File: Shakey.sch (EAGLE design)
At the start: 84 parts, among them CN1 MicroUSB, U1 ATMEGA32U4-AU, U2 ICM-20689, U3 AP2210K-3.3TRG1, U4 LM75AD, Y1 16Mhz

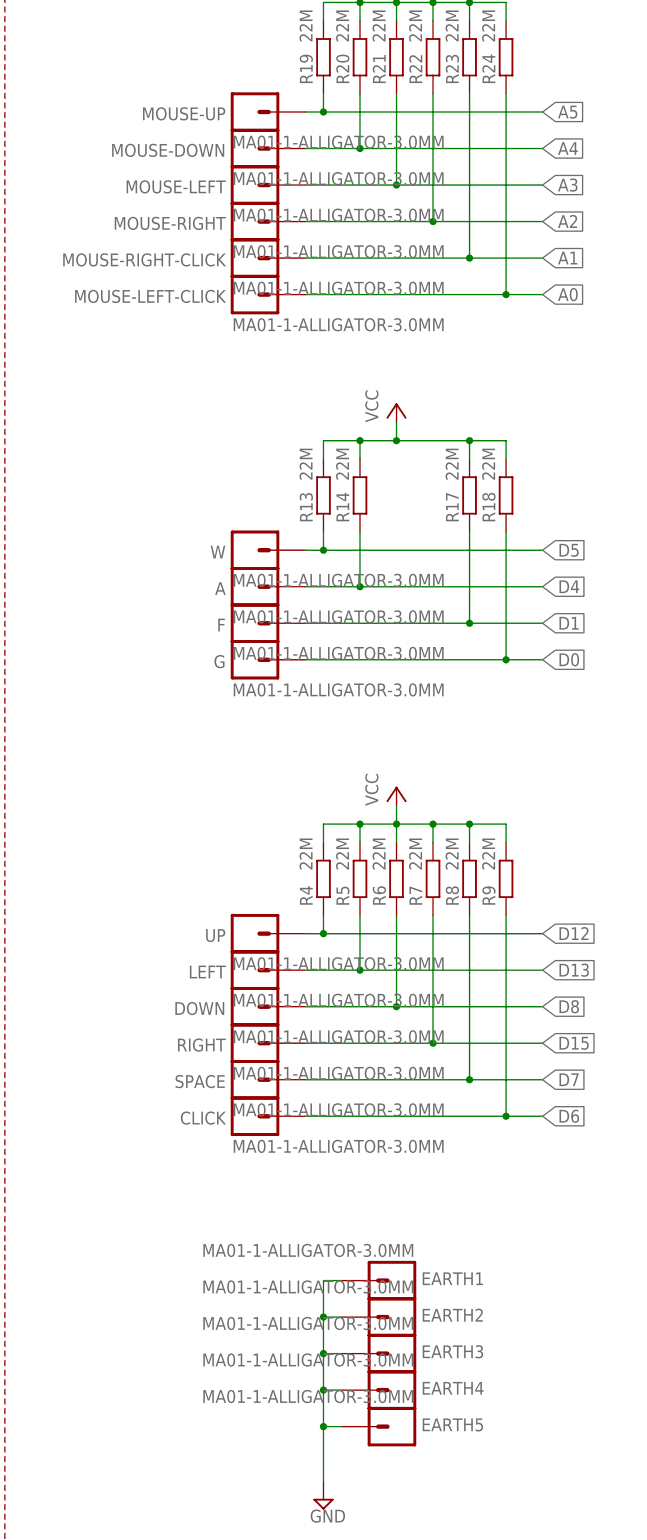
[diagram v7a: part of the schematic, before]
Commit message: added part value for P&P
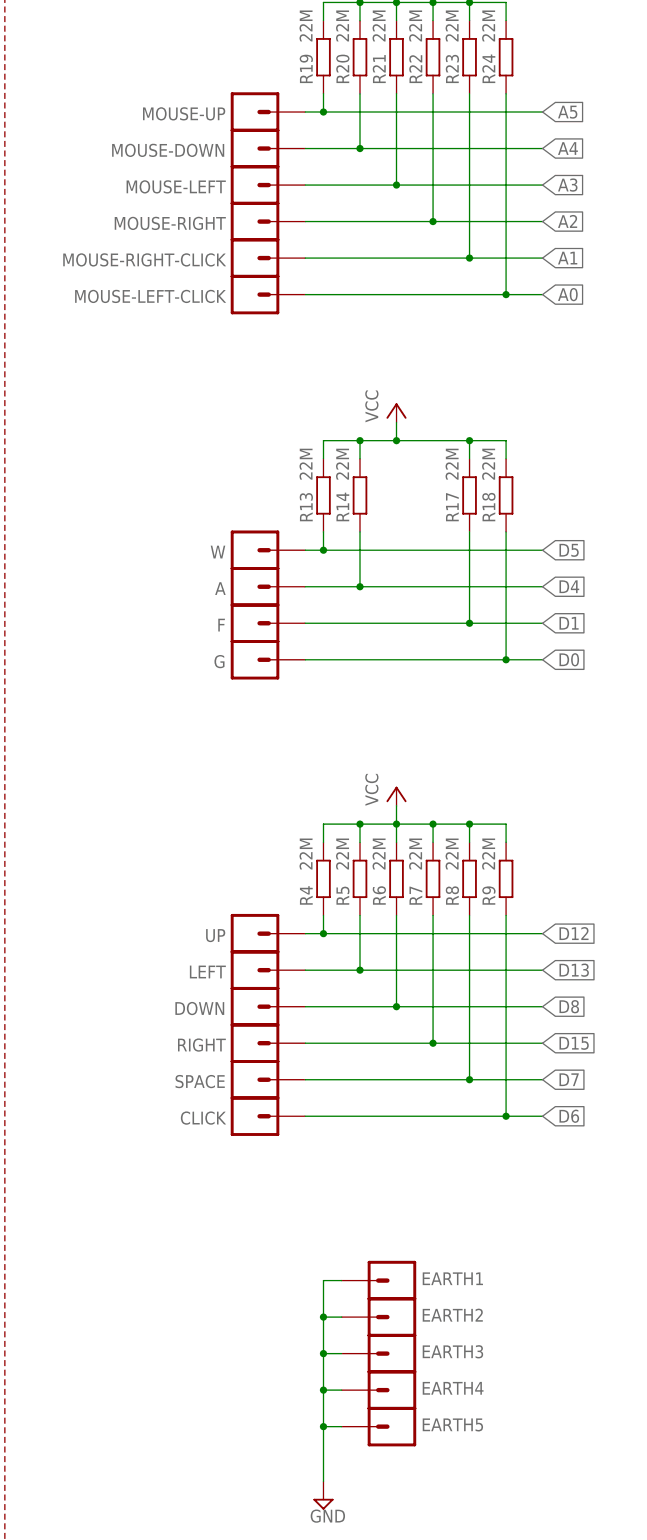
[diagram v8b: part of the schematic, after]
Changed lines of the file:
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@@
 </part>
 <part name="P+3" library="supply1" deviceset="VCC" device=""/>
-<part name="UP" library="SixthLogic" deviceset="MA01-1-ALLIGATOR" device="-3.0MM" value="MA01-1-ALLIGATOR-3.0MM"/>
-<part name="LEFT" library="SixthLogic" deviceset="MA01-1-ALLIGATOR" device="-3.0MM" value="MA01-1-ALLIGATOR-3.0MM"/>
-<part name="DOWN" library="SixthLogic" deviceset="MA01-1-ALLIGATOR" device="-3.0MM" value="MA01-1-ALLIGATOR-3.0MM"/>
-<part name="RIGHT" library="SixthLogic" deviceset="MA01-1-ALLIGATOR" device="-3.0MM" value="MA01-1-ALLIGATOR-3.0MM"/>
-<part name="SPACE" library="SixthLogic" deviceset="MA01-1-ALLIGATOR" device="-3.0MM" value="MA01-1-ALLIGATOR-3.0MM"/>
-<part name="CLICK" library="SixthLogic" deviceset="MA01-1-ALLIGATOR" device="-3.0MM" value="MA01-1-ALLIGATOR-3.0MM"/>
+<part name="UP" library="SixthLogic" deviceset="MA01-1-ALLIGATOR" device="-3.0MM" value=""/>
+<part name="LEFT" library="SixthLogic" deviceset="MA01-1-ALLIGATOR" device="-3.0MM" value=""/>
+<part name="DOWN" library="SixthLogic" deviceset="MA01-1-ALLIGATOR" device="-3.0MM" value=""/>
+<part name="RIGHT" library="SixthLogic" deviceset="MA01-1-ALLIGATOR" device="-3.0MM" value=""/>
+<part name="SPACE" library="SixthLogic" deviceset="MA01-1-ALLIGATOR" device="-3.0MM" value=""/>
+<part name="CLICK" library="SixthLogic" deviceset="MA01-1-ALLIGATOR" device="-3.0MM" value=""/>
 <part name="R4" library="rcl" deviceset="R-EU_" device="R0603" value="22M">
 <attribute name="DESCRIPTION" value="RES SMD 22M OHM 10% 1/10W 0603"/>
@@
 <attribute name="URL" value="https://www.digikey.com/product-detail/en/panasonic-electronic-components/ERJ-3GEYK226V/P22MGTR-ND/282153"/>
 </part>
-<part name="EARTH1" library="SixthLogic" deviceset="MA01-1-ALLIGATOR" device="-3.0MM" value="MA01-1-ALLIGATOR-3.0MM"/>
-<part name="EARTH2" library="SixthLogic" deviceset="MA01-1-ALLIGATOR" device="-3.0MM" value="MA01-1-ALLIGATOR-3.0MM"/>
-<part name="EARTH3" library="SixthLogic" deviceset="MA01-1-ALLIGATOR" device="-3.0MM" value="MA01-1-ALLIGATOR-3.0MM"/>
-<part name="EARTH4" library="SixthLogic" deviceset="MA01-1-ALLIGATOR" device="-3.0MM" value="MA01-1-ALLIGATOR-3.0MM"/>
-<part name="EARTH5" library="SixthLogic" deviceset="MA01-1-ALLIGATOR" device="-3.0MM" value="MA01-1-ALLIGATOR-3.0MM"/>
+<part name="EARTH1" library="SixthLogic" deviceset="MA01-1-ALLIGATOR" device="-3.0MM" value=""/>
+<part name="EARTH2" library="SixthLogic" deviceset="MA01-1-ALLIGATOR" device="-3.0MM" value=""/>
+<part name="EARTH3" library="SixthLogic" deviceset="MA01-1-ALLIGATOR" device="-3.0MM" value=""/>
+<part name="EARTH4" library="SixthLogic" deviceset="MA01-1-ALLIGATOR" device="-3.0MM" value=""/>
+<part name="EARTH5" library="SixthLogic" deviceset="MA01-1-ALLIGATOR" device="-3.0MM" value=""/>
 <part name="SUPPLY7" library="supply2" deviceset="GND" device=""/>
 <part name="LED_DOWN" library="SixthLogic" deviceset="LED" device="-1206-LTST-BOTTOM" value="GREEN">
@@
 <part name="P+5" library="supply1" deviceset="VCC" device=""/>
 <part name="SUPPLY8" library="supply2" deviceset="GND" device=""/>
-<part name="G" library="SixthLogic" deviceset="MA01-1-ALLIGATOR" device="-3.0MM" value="MA01-1-ALLIGATOR-3.0MM"/>
-<part name="F" library="SixthLogic" deviceset="MA01-1-ALLIGATOR" device="-3.0MM" value="MA01-1-ALLIGATOR-3.0MM"/>
-<part name="A" library="SixthLogic" deviceset="MA01-1-ALLIGATOR" device="-3.0MM" value="MA01-1-ALLIGATOR-3.0MM"/>
-<part name="W" library="SixthLogic" deviceset="MA01-1-ALLIGATOR" device="-3.0MM" value="MA01-1-ALLIGATOR-3.0MM"/>
+<part name="G" library="SixthLogic" deviceset="MA01-1-ALLIGATOR" device="-3.0MM" value=""/>
+<part name="F" library="SixthLogic" deviceset="MA01-1-ALLIGATOR" device="-3.0MM" value=""/>
+<part name="A" library="SixthLogic" deviceset="MA01-1-ALLIGATOR" device="-3.0MM" value=""/>
+<part name="W" library="SixthLogic" deviceset="MA01-1-ALLIGATOR" device="-3.0MM" value=""/>
 <part name="R13" library="rcl" deviceset="R-EU_" device="R0603" value="22M">
 <attribute name="DESCRIPTION" value="RES SMD 22M OHM 10% 1/10W 0603"/>
@@
 </part>
 <part name="P+6" library="supply1" deviceset="VCC" device=""/>
-<part name="MOUSE-LEFT-CLICK" library="SixthLogic" deviceset="MA01-1-ALLIGATOR" device="-3.0MM" value="MA01-1-ALLIGATOR-3.0MM"/>
-<part name="MOUSE-RIGHT-CLICK" library="SixthLogic" deviceset="MA01-1-ALLIGATOR" device="-3.0MM" value="MA01-1-ALLIGATOR-3.0MM"/>
-<part name="MOUSE-RIGHT" library="SixthLogic" deviceset="MA01-1-ALLIGATOR" device="-3.0MM" value="MA01-1-ALLIGATOR-3.0MM"/>
-<part name="MOUSE-LEFT" library="SixthLogic" deviceset="MA01-1-ALLIGATOR" device="-3.0MM" value="MA01-1-ALLIGATOR-3.0MM"/>
-<part name="MOUSE-DOWN" library="SixthLogic" deviceset="MA01-1-ALLIGATOR" device="-3.0MM" value="MA01-1-ALLIGATOR-3.0MM"/>
-<part name="MOUSE-UP" library="SixthLogic" deviceset="MA01-1-ALLIGATOR" device="-3.0MM" value="MA01-1-ALLIGATOR-3.0MM"/>
+<part name="MOUSE-LEFT-CLICK" library="SixthLogic" deviceset="MA01-1-ALLIGATOR" device="-3.0MM" value=""/>
+<part name="MOUSE-RIGHT-CLICK" library="SixthLogic" deviceset="MA01-1-ALLIGATOR" device="-3.0MM" value=""/>
+<part name="MOUSE-RIGHT" library="SixthLogic" deviceset="MA01-1-ALLIGATOR" device="-3.0MM" value=""/>
+<part name="MOUSE-LEFT" library="SixthLogic" deviceset="MA01-1-ALLIGATOR" device="-3.0MM" value=""/>
+<part name="MOUSE-DOWN" library="SixthLogic" deviceset="MA01-1-ALLIGATOR" device="-3.0MM" value=""/>
+<part name="MOUSE-UP" library="SixthLogic" deviceset="MA01-1-ALLIGATOR" device="-3.0MM" value=""/>
 <part name="R19" library="rcl" deviceset="R-EU_" device="R0603" value="22M">
 <attribute name="DESCRIPTION" value="RES SMD 22M OHM 10% 1/10W 0603"/>
@@
 <instance part="JP1" gate="G$1" x="374.396" y="11.43"/>
 <instance part="U$10" gate="G$1" x="0" y="0"/>
-<instance part="TP1" gate="G$1" x="68.58" y="231.14"/>
+<instance part="TP1" gate="G$1" x="68.58" y="231.14" smashed="yes">
+<attribute name="NAME" x="67.31" y="232.41" size="1.778" layer="95"/>
+</instance>
 </instances>
 <busses>
